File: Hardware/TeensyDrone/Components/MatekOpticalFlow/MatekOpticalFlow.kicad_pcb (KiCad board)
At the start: 2 copper layers, 4 parts, among them J1 Conn_02x02_Odd_Even, U1 STM32L051C8Tx

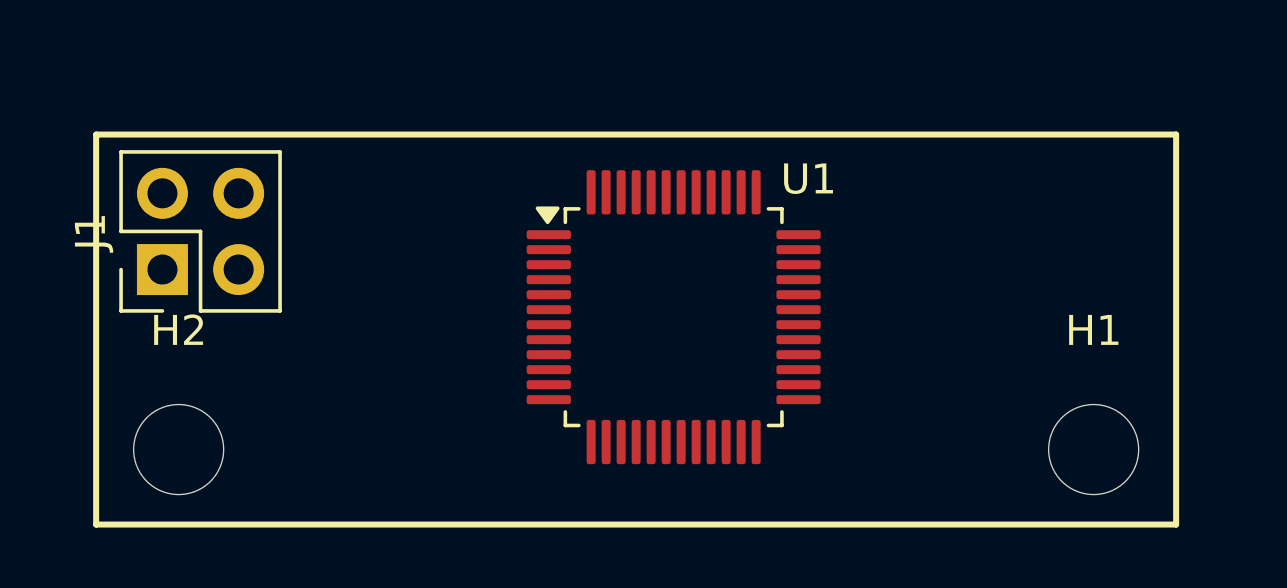
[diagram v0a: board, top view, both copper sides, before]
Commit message: Moved to Teensy 4.0 from 4.1
Signed-off-by: lucas <mtglucas1@gmail.com>
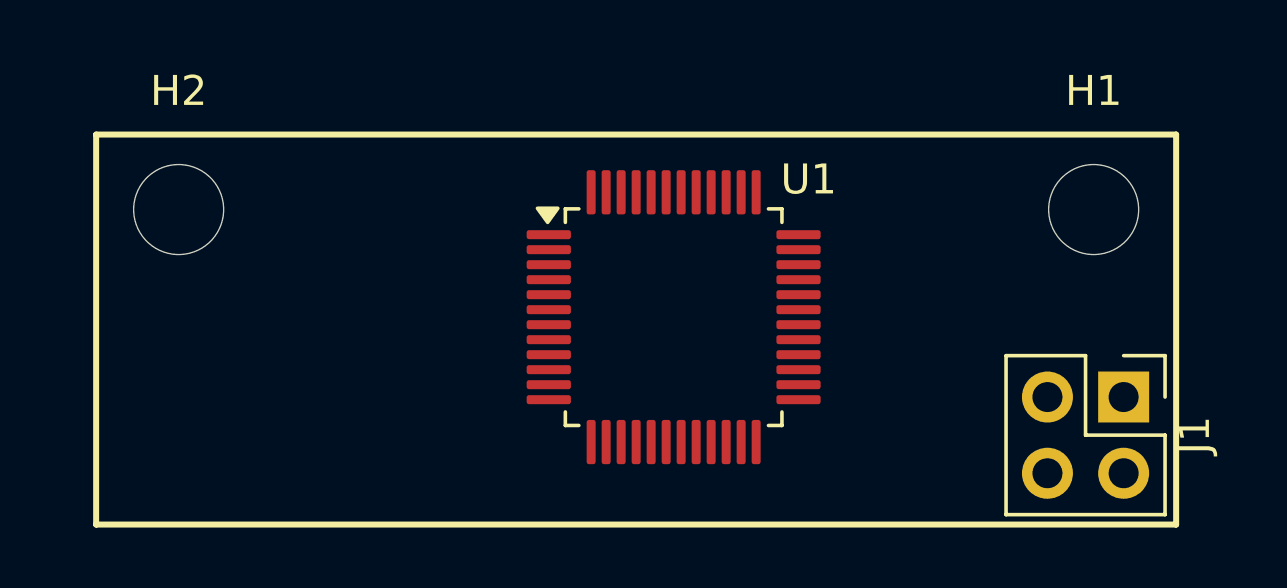
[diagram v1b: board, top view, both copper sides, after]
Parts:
- moved J1 32.3 mm to (71.8, 76.2), turned to -90 degrees
- moved H1 8.00 mm to (70.8, 70.0)
- moved H2 8.00 mm to (40.2, 70.0)

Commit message: Revert "Moved to Teensy 4.0 from 4.1"
This reverts commit 64f42becbd12878e856e1dc259d1d069ff850610.
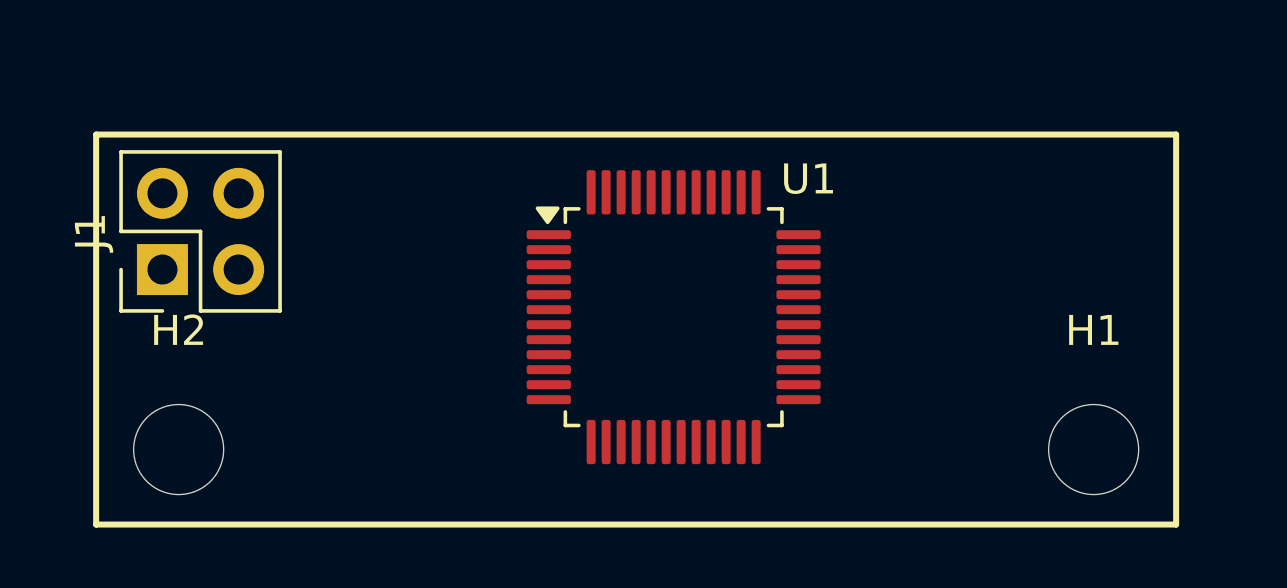
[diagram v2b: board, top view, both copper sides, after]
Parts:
- moved J1 32.3 mm to (39.7, 72.0), turned to 90 degrees
- moved H1 8.00 mm to (70.8, 78.0)
- moved H2 8.00 mm to (40.2, 78.0)
